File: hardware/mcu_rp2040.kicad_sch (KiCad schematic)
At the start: 30 parts, among them SW1 PTS815 SJM 250 SMTR LFS, U1 RP2040, U2 W25Q128JVSIQ, X1 ABM8AIG-12.000MHZ-12-2Z-T3

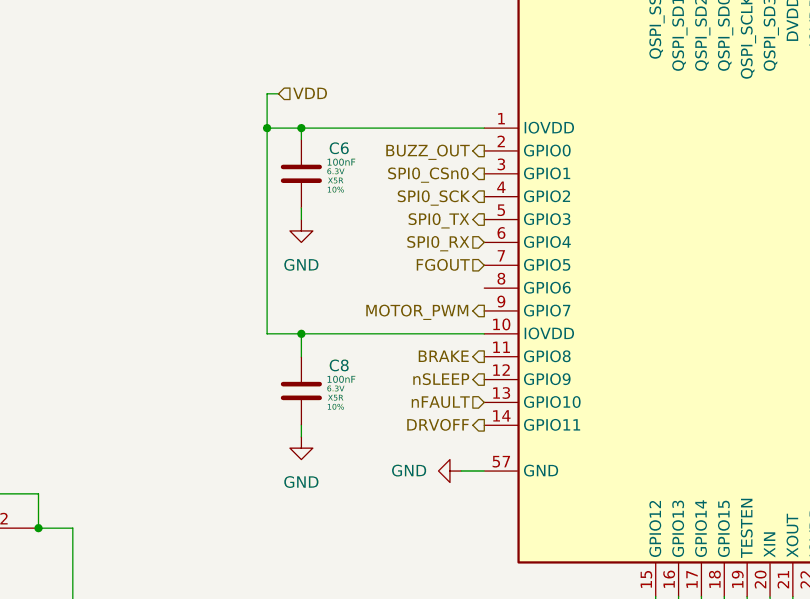
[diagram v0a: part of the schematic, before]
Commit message: version of pcb with no motor driver, only previously used servo enable and pwm circuit
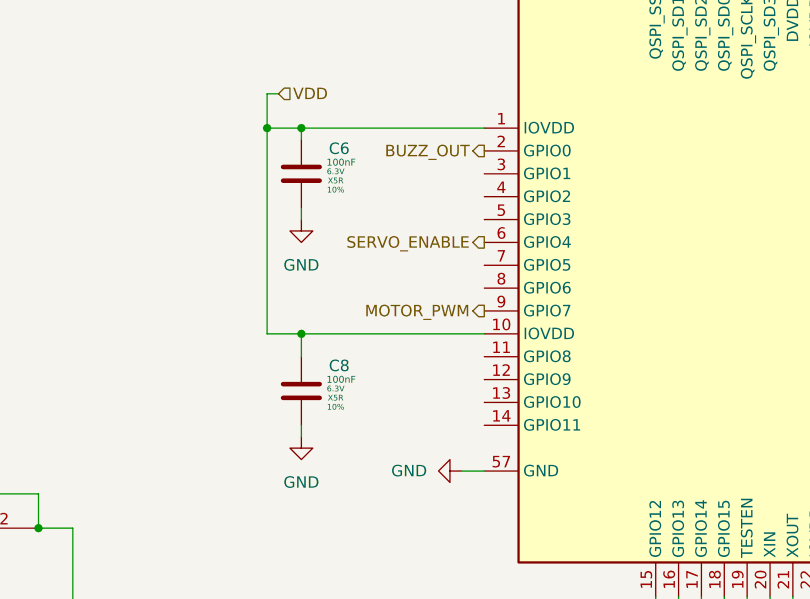
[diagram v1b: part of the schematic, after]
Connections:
- net BRAKE: no longer names the net of U1.11 (GPIO8)
- net DRVOFF: no longer names the net of U1.14 (GPIO11)
- net FGOUT: no longer names the net of U1.7 (GPIO5)
- net SPI0_CSn0: no longer names the net of U1.3 (GPIO1)
- net SPI0_RX renamed SERVO_ENABLE
- net SPI0_SCK: no longer names the net of U1.4 (GPIO2)
- net SPI0_TX: no longer names the net of U1.5 (GPIO3)
- net nFAULT: no longer names the net of U1.13 (GPIO10)
- net nSLEEP: no longer names the net of U1.12 (GPIO9)
